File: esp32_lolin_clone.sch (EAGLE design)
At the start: 33 parts, among them J1 10104111-0001LF, P1 S2B-PH-SM4-TB, Q1 CJ2301S1, Q2 CJ2301S1, SW1 PTS815SJK250SMTR, U1 ESP32-WROOM-32D, U2 BCM857, U3 ME6211, U4 UMH3N, U5 TP4054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

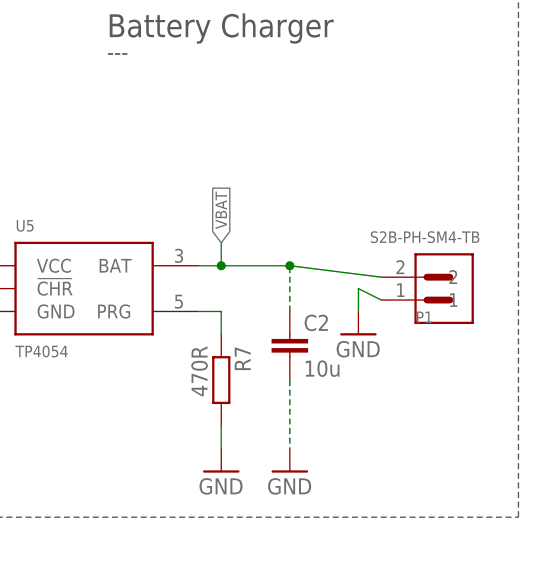
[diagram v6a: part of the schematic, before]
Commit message: - FIX CRITICAL ERROR: Battery connector pins were swapped.
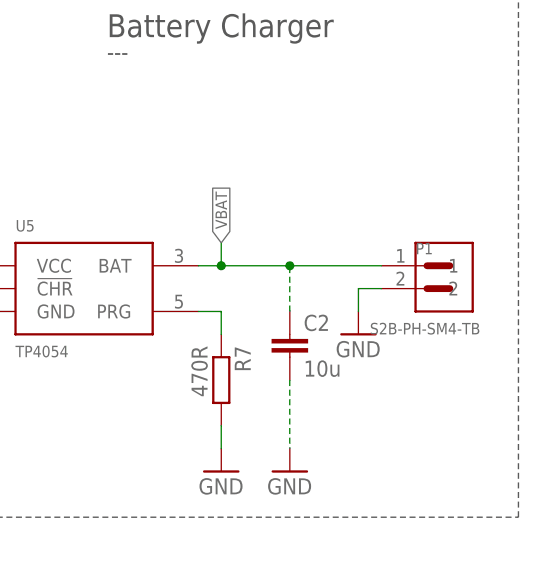
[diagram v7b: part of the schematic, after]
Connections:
- net GND: now also P1.2; no longer P1.1
- net VBAT: now also P1.1; no longer P1.2
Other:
- moved on the sheet: P1
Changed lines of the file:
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@@
 <attribute name="VALUE" x="339.598" y="212.09" size="1.778" layer="96" rot="R270"/>
 </instance>
-<instance part="P1" gate="G$1" x="365.76" y="219.71" smashed="yes" rot="MR180">
-<attribute name="NAME" x="364.48818125" y="215.89453125" size="1.27181875" layer="95" rot="MR180"/>
-<attribute name="VALUE" x="359.40901875" y="224.79391875" size="1.27098125" layer="96" rot="MR180"/>
+<instance part="P1" gate="G$1" x="365.76" y="218.44" smashed="yes">
+<attribute name="NAME" x="364.48818125" y="222.25546875" size="1.27181875" layer="95"/>
+<attribute name="VALUE" x="359.40901875" y="213.35608125" size="1.27098125" layer="96"/>
 </instance>
 <instance part="GND11" gate="1" x="342.9" y="198.12" smashed="yes">
@@
 </segment>
 <segment>
-<pinref part="P1" gate="G$1" pin="1"/>
-<wire x1="360.68" y1="217.17" x2="358.14" y2="218.44" width="0.1524" layer="91"/>
-<wire x1="358.14" y1="218.44" x2="358.14" y2="215.9" width="0.1524" layer="91"/>
-<pinref part="GND12" gate="1" pin="GND"/>
-</segment>
-<segment>
 <pinref part="U6" gate="IC" pin="GND"/>
 <pinref part="GND13" gate="1" pin="GND"/>
@@
 <wire x1="350.52" y1="208.28" x2="350.52" y2="200.66" width="0.1524" layer="91" style="longdash"/>
 <pinref part="GND22" gate="1" pin="GND"/>
+</segment>
+<segment>
+<pinref part="GND12" gate="1" pin="GND"/>
+<wire x1="358.14" y1="215.9" x2="358.14" y2="218.44" width="0.1524" layer="91"/>
+<pinref part="P1" gate="G$1" pin="2"/>
+<wire x1="358.14" y1="218.44" x2="360.68" y2="218.44" width="0.1524" layer="91"/>
 </segment>
 </net>
@@
 <wire x1="342.9" y1="220.98" x2="342.9" y2="223.52" width="0.1524" layer="91"/>
 <label x="342.9" y="223.52" size="1.27" layer="95" rot="R90" xref="yes"/>
-<pinref part="P1" gate="G$1" pin="2"/>
-<wire x1="360.68" y1="219.71" x2="350.52" y2="220.98" width="0.1524" layer="91"/>
 <junction x="342.9" y="220.98"/>
 <pinref part="C2" gate="G$1" pin="1"/>
 <wire x1="350.52" y1="220.98" x2="342.9" y2="220.98" width="0.1524" layer="91"/>
 <wire x1="350.52" y1="215.9" x2="350.52" y2="220.98" width="0.1524" layer="91" style="longdash"/>
+<pinref part="P1" gate="G$1" pin="1"/>
+<wire x1="350.52" y1="220.98" x2="360.68" y2="220.98" width="0.1524" layer="91"/>
 <junction x="350.52" y="220.98"/>
 </segment>
